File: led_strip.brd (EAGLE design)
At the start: 38.5 x 15.8 mm, 18 parts, among them IC1 REG1117, IC2 MEGA8-AI, U1 MIC9.7MM, Y1 16MHz

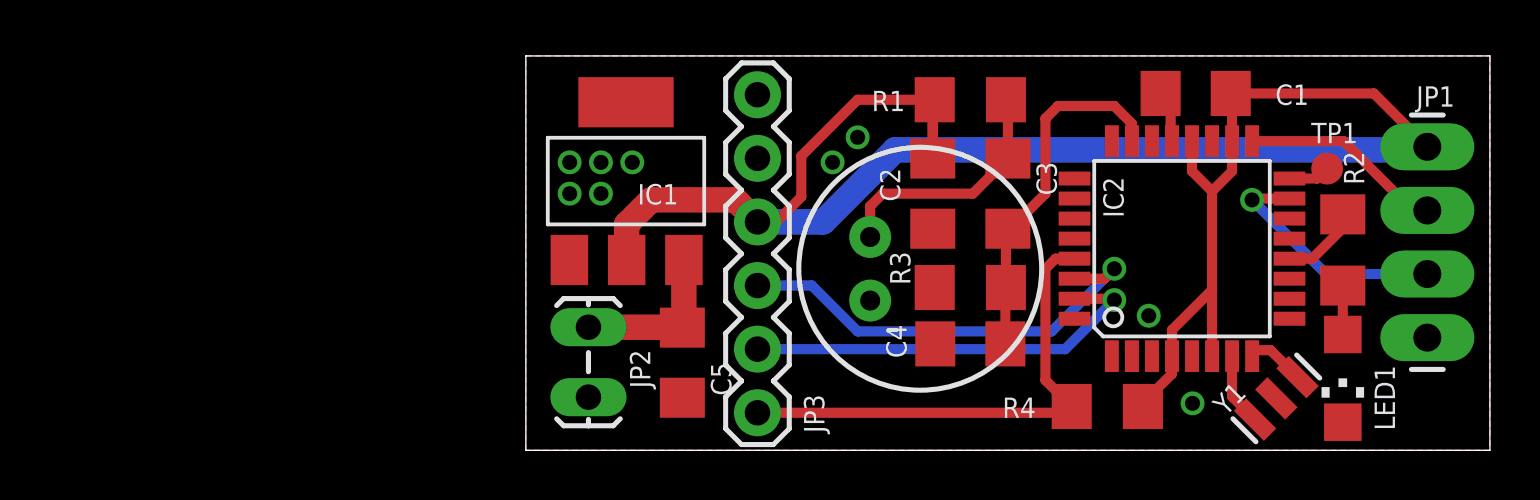
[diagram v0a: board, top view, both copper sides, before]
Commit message: Added DTR capacitor for programming, reversed SPI header for LED stip.
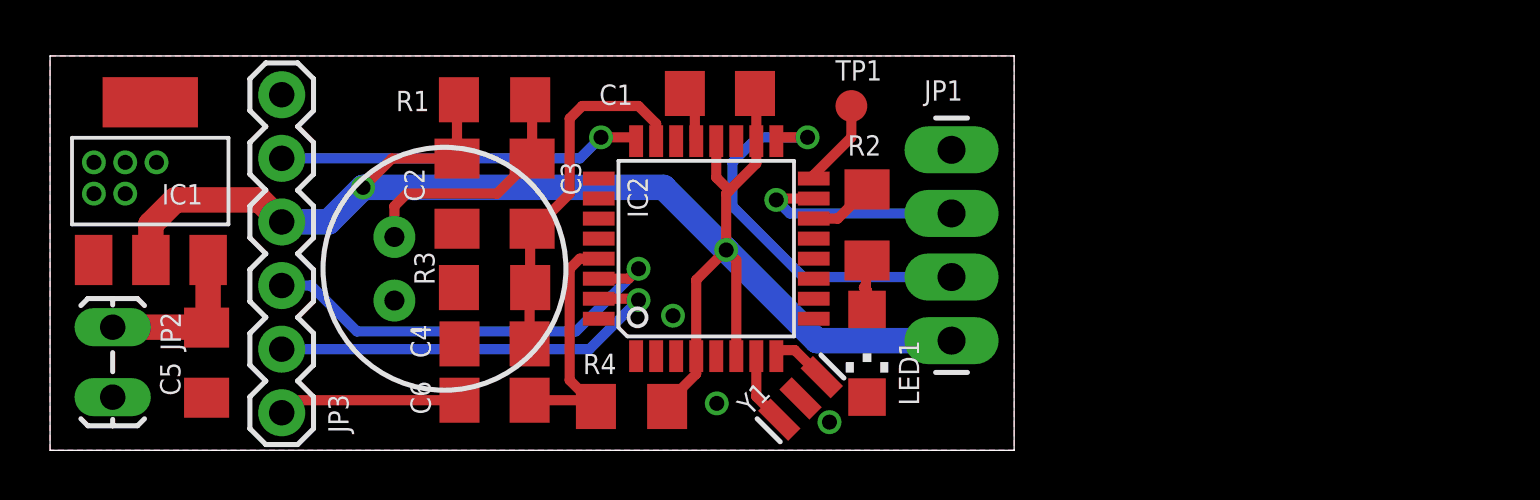
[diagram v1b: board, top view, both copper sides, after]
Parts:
- added C6: 0.1uf, adafruit:C1206
- moved JP1 20.4 mm to (36.0, 12.0), turned to 270 degrees
- moved TP1 19.2 mm to (32.0, 13.8)
- moved LED1 19.0 mm to (32.6, 3.88)
- moved R2 19.0 mm to (32.6, 9.00)
- moved C1 19.0 mm to (26.8, 14.2)
- moved C2 19.0 mm to (16.2, 10.2)
- moved C3 19.0 mm to (19.2, 10.2)
- moved C4 19.0 mm to (17.8, 4.25)
- moved C5 19.0 mm to (6.25, 3.50)
- moved IC1 19.0 mm to (4.00, 10.8)
- moved IC2 19.0 mm to (26.2, 8.05)
- moved JP2 19.0 mm to (2.50, 2.25)
- moved JP3 19.0 mm to (9.25, 1.50)
- moved R1 19.0 mm to (17.8, 14.0)
- moved R3 19.0 mm to (17.8, 6.50)
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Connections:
- new net N$11: C6.2, JP3.DTR
- new net N$12: IC2.24, JP3.CTS
- net N$18: now also IC2.14; no longer IC2.12
- net N$7: now also C6.1; no longer JP3.DTR
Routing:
- net N$12: track 0.00 -> 14.6 mm, vias 0 -> 1
- net VCC: track 77.9 -> 65.0 mm, vias 0 -> 2
- net N$7: track 20.3 -> 10.6 mm
- net N$1: track 8.14 -> 16.4 mm, vias 0 -> 1
- net N$11: track 0.00 -> 7.31 mm
- net N$2: track 1.67 -> 3.77 mm
- net N$3: track 9.74 -> 8.74 mm
- net N$18: track 3.18 -> 2.61 mm
- net GND: vias 9 -> 8

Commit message: Updated BOM, fixed LED current limiting resistor to sane value.
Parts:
- R2: value 10k -> 330
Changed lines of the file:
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@@
 <attribute name="VALUE" x="30.085" y="5.145" size="1.27" layer="27" rot="R270"/>
 </element>
-<element name="R2" library="adafruit" package="R1206" value="10k" x="32.625" y="9" smashed="yes" rot="R90">
+<element name="R2" library="adafruit" package="R1206" value="330" x="32.625" y="9" smashed="yes" rot="R90">
 <attribute name="NAME" x="31.853" y="11.768" size="0.8128" layer="25" font="vector"/>
 <attribute name="VALUE" x="35.038" y="7.603" size="1.27" layer="27" rot="R90"/>

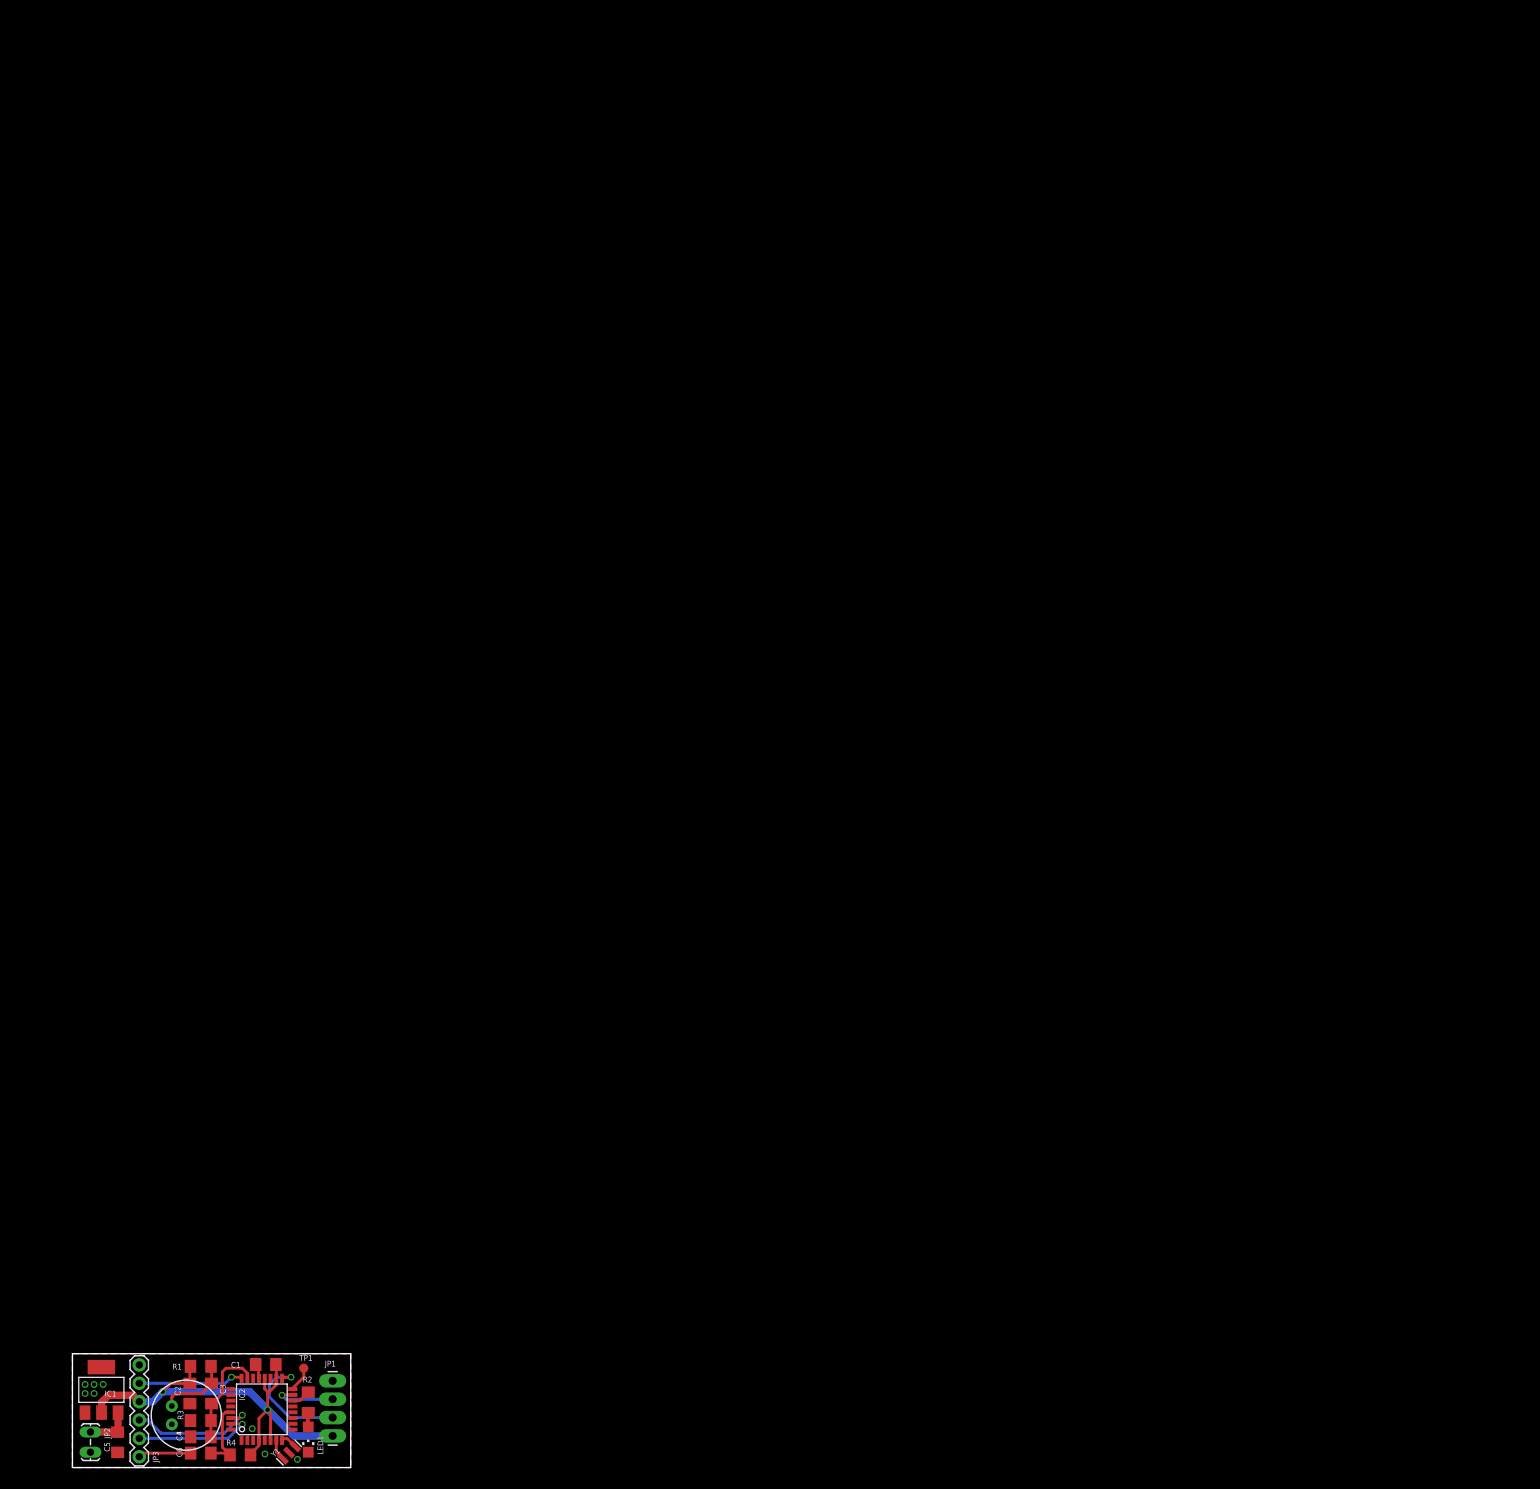
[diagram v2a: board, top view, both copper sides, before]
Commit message: Created usb bootloader varient.
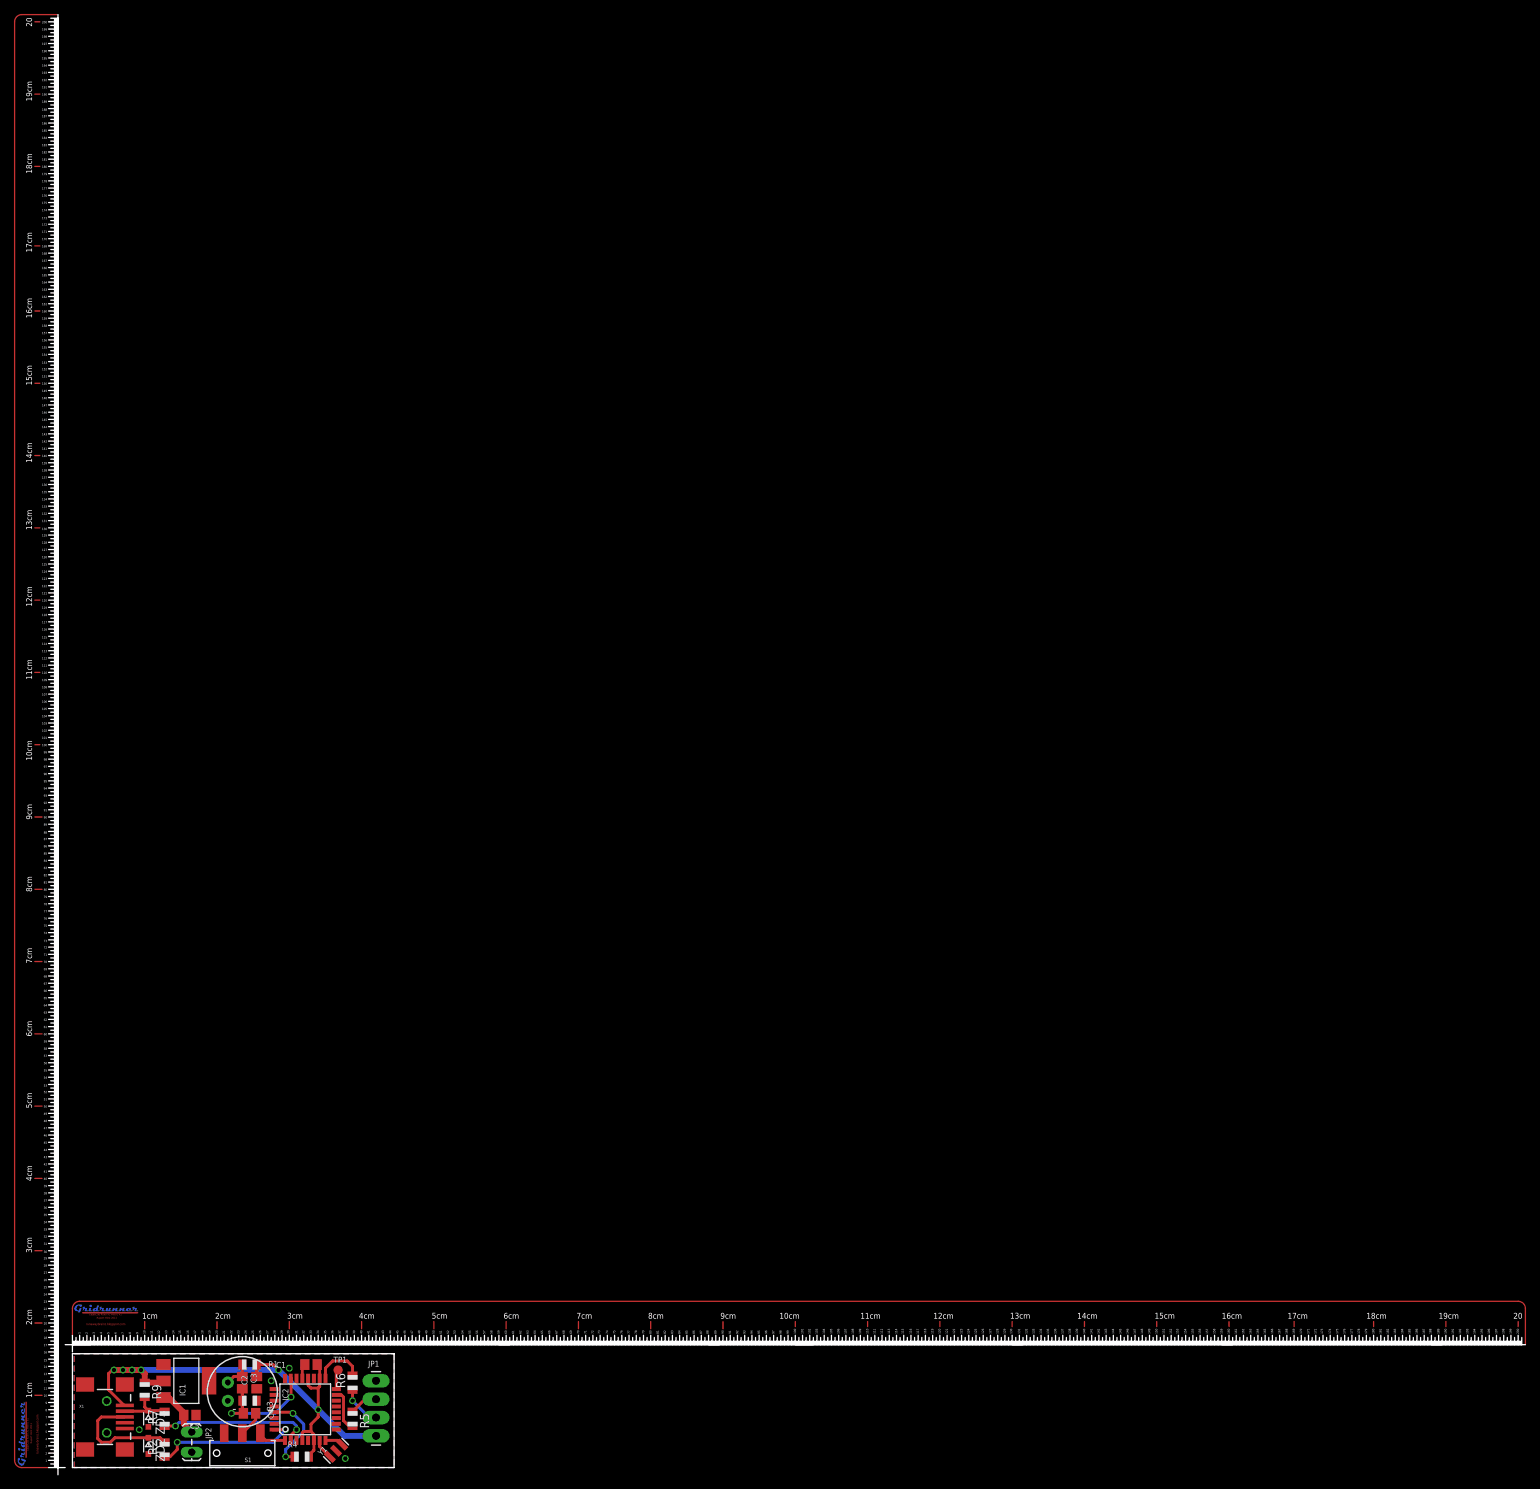
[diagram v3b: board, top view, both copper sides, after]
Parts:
- removed C6: 0.1uf, adafruit:C1206
- removed JP3: FTDI_BASICPTH, sparkfun:FTDI_BASIC
- removed LED1: (no value), adafruit:CHIPLED_1206
- added R5, R6: 330, adafruit:R0805
- added R7: 68, adafruit:R0805
- added R9: 1.5k, adafruit:R0805
- added S1: (no value), sparkfun:SWITCH-SPDT-SMD
- added U$1, U$2: (no value), CAD Ruler_EagleCad Gridrunner XL Metric V1 (Rupert Hirst 2011):RULER
- added X1: USB-SMD-NS, sparkfun:USB-MINIB-NOSTOP
- added ZD1, ZD2: (no value), dp_devices:SOD-323F
- C1, C2, C3, C4, C5: device adafruit:C1206 -> adafruit:C0805
- R1, R3, R4: device adafruit:R1206 -> adafruit:R0805
- R2: value 330 -> 68; device adafruit:R1206 -> adafruit:R0805
- moved R2 20.9 mm to (12.8, 2.50)
- moved JP2 14.0 mm to (16.5, 2.25)
- moved IC1 11.8 mm to (15.8, 12.0), turned to 270 degrees
- moved C5 10.7 mm to (16.2, 7.25), turned to 0 degrees
- moved C2 9.37 mm to (25.5, 11.8)
- moved R4 8.50 mm to (31.7, 1.50)
- moved U1 8.40 mm to (23.5, 10.5)
- moved C4 7.49 mm to (24.5, 7.50), turned to 0 degrees
- moved R3 7.29 mm to (24.5, 9.25), turned to 180 degrees
- moved R1 6.75 mm to (24.5, 14.2), turned to 0 degrees
- moved Y1 6.50 mm to (36.5, 2.32)
- moved C1 6.25 mm to (33.0, 14.2)
- moved IC2 6.00 mm to (32.2, 8.05)
- moved JP1 6.00 mm to (42.0, 12.0)
- moved TP1 4.76 mm to (36.8, 13.5)
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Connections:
- removed net N$18: IC2.14, R2.2
- new net N$14: JP1.3, R6.1
- new net N$15: IC2.15, R5.2
- net GND: now also S1.2, X1.GND, ZD1.A, ZD2.A; no longer JP3.GND, LED1.C
- net N$1: now also R6.2; no longer JP1.3
- net N$11: now also IC2.2, R7.1; no longer C6.2, JP3.DTR
- net N$12: now also IC2.32, R2.1; no longer IC2.24, JP3.CTS
- net N$13: now also IC2.1, S1.1; no longer LED1.A, R2.1
- net N$3: now also R5.1; no longer IC2.15
- net N$4: now also R2.2, X1.D+, ZD2.C; no longer IC2.30, JP3.TXO
- net N$5: now also R7.2, R9.2, X1.D-, ZD1.C; no longer IC2.31, JP3.RXI
- net N$7: no longer C6.1
- net VCC: now also R9.1, X1.VBUS; no longer JP3.VCC
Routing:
- net VCC: track 65.0 -> 80.3 mm, vias 2 -> 6
- net N$11: track 7.31 -> 21.0 mm, vias 0 -> 2
- net N$1: track 16.4 -> 7.13 mm, vias 1 -> 0
- net N$5: track 16.7 -> 7.66 mm, vias 1 -> 0
- net N$12: track 14.6 -> 20.7 mm, vias 1 -> 2
- net N$15: track 0.00 -> 5.94 mm
- net N$10: track 9.90 -> 3.99 mm
- net N$9: track 14.4 -> 20.2 mm, vias 0 -> 2
- net N$14: track 0.00 -> 5.72 mm, vias 0 -> 1
- net N$3: track 8.74 -> 3.96 mm, vias 1 -> 0
- net GND: track 2.11 -> 5.56 mm, vias 8 -> 4
- net N$18: track 2.61 -> 0.00 mm
- net N$13: track 2.04 -> 3.96 mm
- net N$4: track 17.8 -> 16.4 mm, vias 1 -> 0
- net N$2: track 3.77 -> 2.75 mm
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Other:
- board size 38.5 x 15.8 mm -> 44.5 x 15.8 mm
